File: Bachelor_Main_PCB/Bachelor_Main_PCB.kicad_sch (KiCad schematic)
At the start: 4 parts

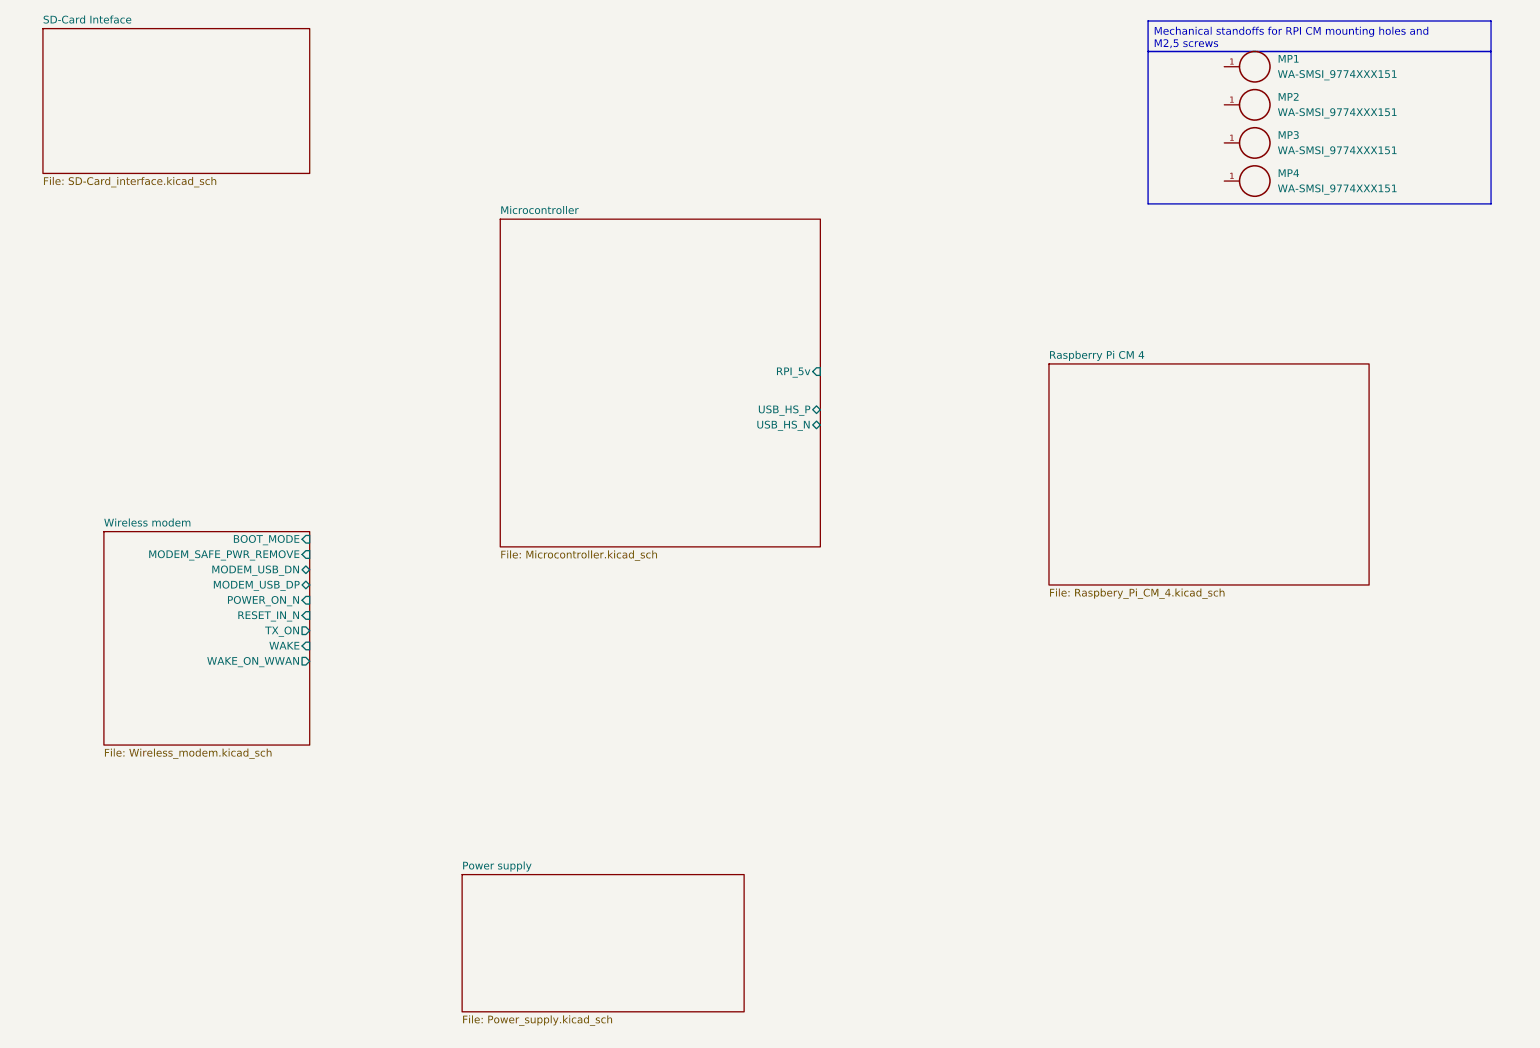
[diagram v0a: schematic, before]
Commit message: Add routing between hierarchal sheets modem and RPI
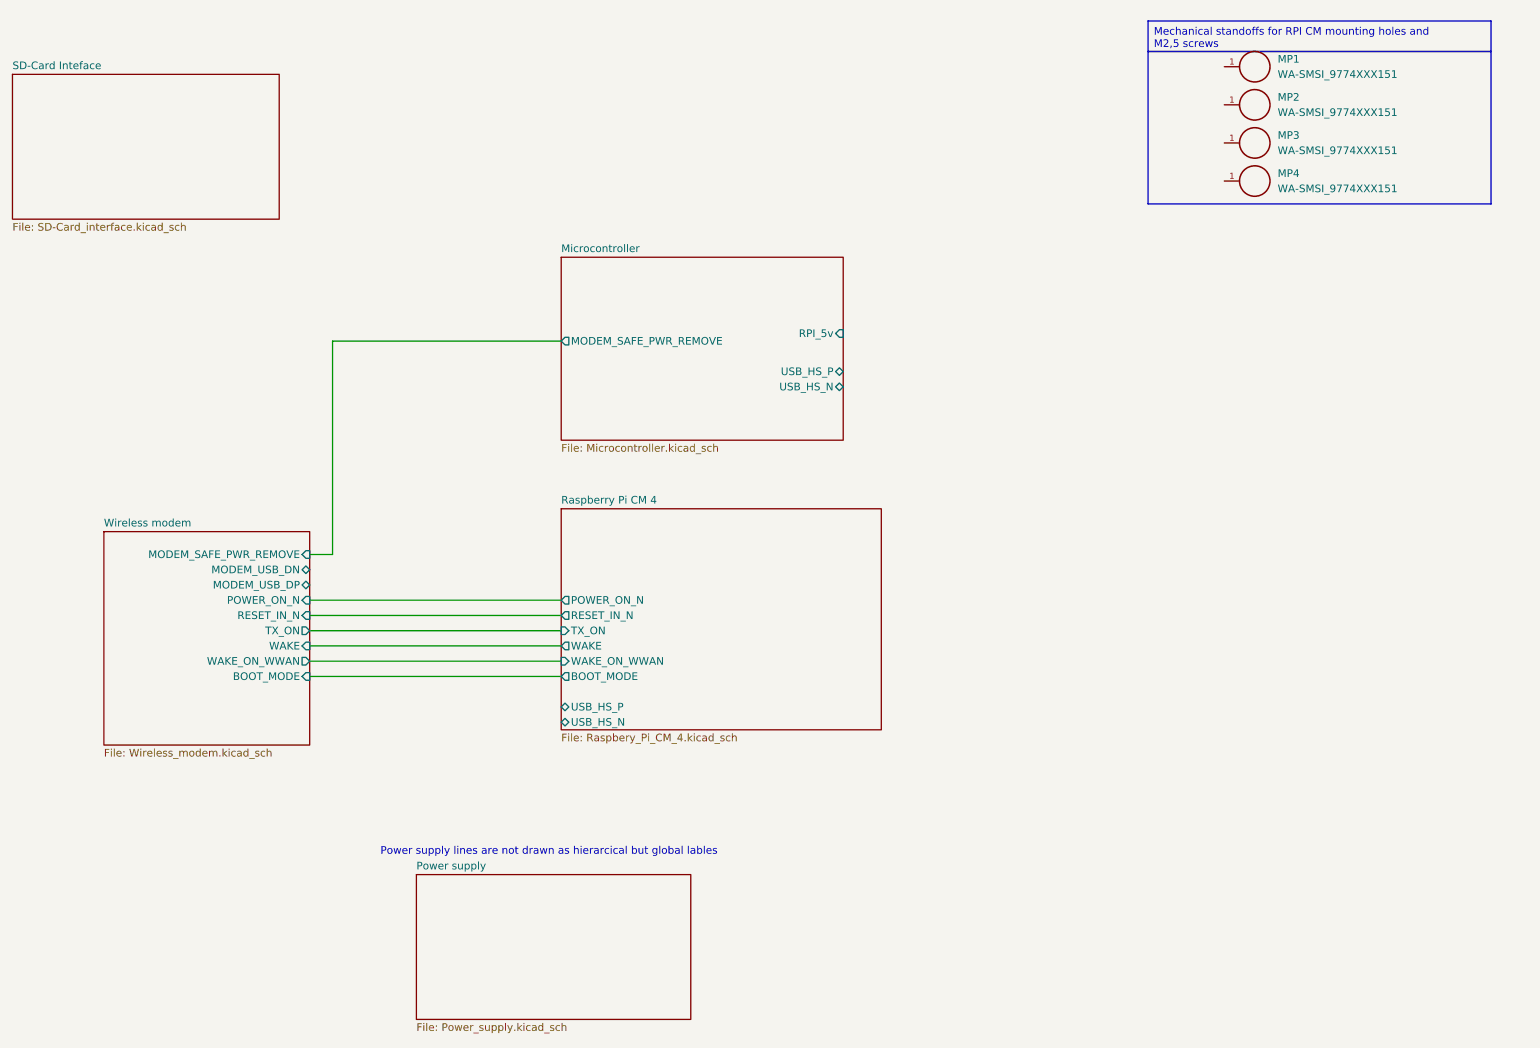
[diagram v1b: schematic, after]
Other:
- sheet Microcontroller ports: added MODEM_SAFE_PWR_REMOVE; removed none
- sheet Raspberry Pi CM 4 ports: added BOOT_MODE, POWER_ON_N, RESET_IN_N, TX_ON, USB_HS_N, USB_HS_P, WAKE, WAKE_ON_WWAN; removed none
- note added: "Power supply lines are not drawn as hierarcical but global lables"
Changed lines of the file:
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@@
 	(generator_version "9.0")
 	(paper "A4")
+	(text "Power supply lines are not drawn as hierarcical but global lables"
+		(exclude_from_sim no)
+		(at 119.888 156.21 0)
+		(effects
+			(font
+				(size 1.27 1.27)
+			)
+		)
+	)
 	(text_box " "
 		(exclude_from_sim no)
@@
 			)
 			(justify left top)
+		)
+	)
+	(wire
+		(pts
+			(xy 80.01 106.68) (xy 83.82 106.68)
+		)
+		(stroke
+			(width 0)
+			(type default)
+		)
+	)
+	(wire
+		(pts
+			(xy 83.82 71.12) (xy 121.92 71.12)
+		)
+		(stroke
+			(width 0)
+			(type default)
+		)
+	)
+	(wire
+		(pts
+			(xy 80.01 114.3) (xy 121.92 114.3)
+		)
+		(stroke
+			(width 0)
+			(type default)
+		)
+	)
+	(wire
+		(pts
+			(xy 80.01 127) (xy 121.92 127)
+		)
+		(stroke
+			(width 0)
+			(type default)
+		)
+	)
+	(wire
+		(pts
+			(xy 80.01 124.46) (xy 121.92 124.46)
+		)
+		(stroke
+			(width 0)
+			(type default)
+		)
+	)
+	(wire
+		(pts
+			(xy 83.82 106.68) (xy 83.82 71.12)
+		)
+		(stroke
+			(width 0)
+			(type default)
+		)
+	)
+	(wire
+		(pts
+			(xy 80.01 116.84) (xy 121.92 116.84)
+		)
+		(stroke
+			(width 0)
+			(type default)
+		)
+	)
+	(wire
+		(pts
+			(xy 80.01 121.92) (xy 121.92 121.92)
+		)
+		(stroke
+			(width 0)
+			(type default)
+		)
+	)
+	(wire
+		(pts
+			(xy 80.01 119.38) (xy 121.92 119.38)
+		)
+		(stroke
+			(width 0)
+			(type default)
 		)
 	)
@@
 		)
 		(pin "BOOT_MODE" input
-			(at 80.01 104.14 0)
+			(at 80.01 127 0)
 			(effects
 				(font
@@
 	)
 	(sheet
-		(at 203.2 74.93)
+		(at 121.92 99.06)
 		(size 53.34 36.83)
 		(exclude_from_sim no)
@@
 		)
 		(property "Sheetname" "Raspberry Pi CM 4"
-			(at 203.2 74.2184 0)
+			(at 121.92 98.3484 0)
 			(effects
 				(font
@@
 		)
 		(property "Sheetfile" "Raspbery_Pi_CM_4.kicad_sch"
-			(at 203.2 112.3446 0)
+			(at 121.92 136.4746 0)
 			(effects
 				(font
@@
 				)
 				(justify left top)
+			)
+		)
+		(pin "BOOT_MODE" output
+			(at 121.92 127 180)
+			(effects
+				(font
+					(size 1.27 1.27)
+				)
+				(justify left)
+			)
+		)
+		(pin "POWER_ON_N" output
+			(at 121.92 114.3 180)
+			(effects
+				(font
+					(size 1.27 1.27)
+				)
+				(justify left)
+			)
+		)
+		(pin "RESET_IN_N" output
+			(at 121.92 116.84 180)
+			(effects
+				(font
+					(size 1.27 1.27)
+				)
+				(justify left)
+			)
+		)
+		(pin "TX_ON" input
+			(at 121.92 119.38 180)
+			(effects
+				(font
+					(size 1.27 1.27)
+				)
+				(justify left)
+			)
+		)
+		(pin "USB_HS_N" bidirectional
+			(at 121.92 134.62 180)
+			(effects
+				(font
+					(size 1.27 1.27)
+				)
+				(justify left)
+			)
+		)
+		(pin "USB_HS_P" bidirectional
+			(at 121.92 132.08 180)
+			(effects
+				(font
+					(size 1.27 1.27)
+				)
+				(justify left)
+			)
+		)
+		(pin "WAKE" output
+			(at 121.92 121.92 180)
+			(effects
+				(font
+					(size 1.27 1.27)
+				)
+				(justify left)
+			)
+		)
+		(pin "WAKE_ON_WWAN" input
+			(at 121.92 124.46 180)
+			(effects
+				(font
+					(size 1.27 1.27)
+				)
+				(justify left)
 			)
 		)
@@
 	)
 	(sheet
-		(at 105.41 160.02)
-		(size 46.99 22.86)
+		(at 97.79 160.02)
+		(size 45.72 24.13)
 		(exclude_from_sim no)
 		(in_bom yes)
@@
 		)
 		(property "Sheetname" "Power supply"
-			(at 105.41 159.3084 0)
+			(at 97.79 159.3084 0)
 			(effects
 				(font
@@
 		)
 		(property "Sheetfile" "Power_supply.kicad_sch"
-			(at 105.41 183.4646 0)
+			(at 97.79 184.7346 0)
 			(effects
 				(font
@@
 	)
 	(sheet
-		(at 111.76 50.8)
-		(size 53.34 54.61)
+		(at 121.92 57.15)
+		(size 46.99 30.48)
 		(exclude_from_sim no)
 		(in_bom yes)
@@
 		)
 		(property "Sheetname" "Microcontroller"
-			(at 111.76 50.0884 0)
+			(at 121.92 56.4384 0)
 			(effects
 				(font
@@
 		)
 		(property "Sheetfile" "Microcontroller.kicad_sch"
-			(at 111.76 105.9946 0)
+			(at 121.92 88.2146 0)
 			(effects
 				(font
@@
 		)
 		(pin "RPI_5v" input
-			(at 165.1 76.2 0)
+			(at 168.91 69.85 0)
 			(effects
 				(font
@@
 		)
 		(pin "USB_HS_N" bidirectional
-			(at 165.1 85.09 0)
+			(at 168.91 78.74 0)
 			(effects
 				(font
@@
 		)
 		(pin "USB_HS_P" bidirectional
-			(at 165.1 82.55 0)
+			(at 168.91 76.2 0)
 			(effects
 				(font
@@
 				)
 				(justify right)
+			)
+		)
+		(pin "MODEM_SAFE_PWR_REMOVE" output
+			(at 121.92 71.12 180)
+			(effects
+				(font
+					(size 1.27 1.27)
+				)
+				(justify left)
 			)
 		)
@@
 	)
 	(sheet
-		(at 35.56 19.05)
+		(at 30.48 26.67)
 		(size 44.45 24.13)
 		(exclude_from_sim no)
@@
 		)
 		(property "Sheetname" "SD-Card Inteface"
-			(at 35.56 18.3384 0)
+			(at 30.48 25.9584 0)
 			(effects
 				(font
@@
 		)
 		(property "Sheetfile" "SD-Card_interface.kicad_sch"
-			(at 35.56 43.7646 0)
-			(effects
-				(font
+			(at 30.48 51.3846 0)
+			(effects
+				(font

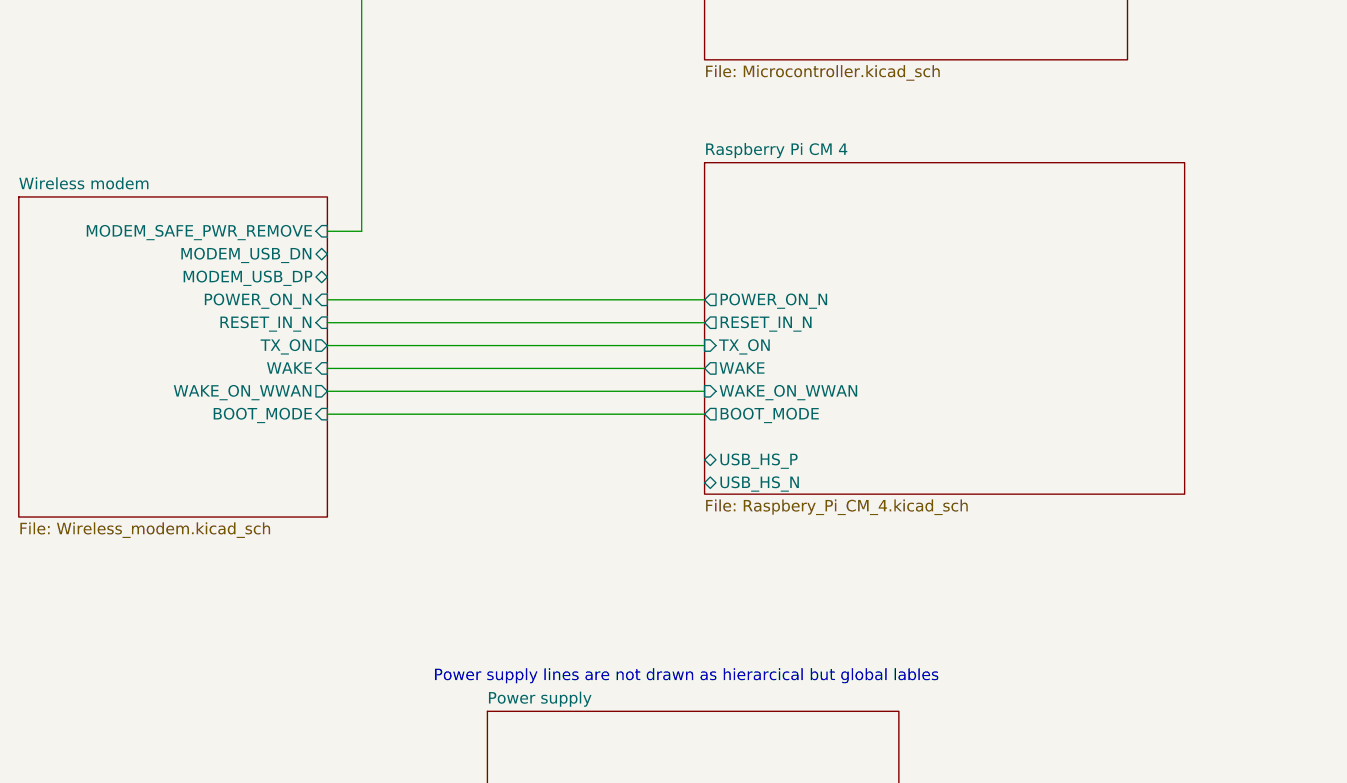
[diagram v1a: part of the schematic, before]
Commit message: Add MODEM_3V5_EN mosfet
Controlls the power supply to the modem from the RPI GPIO7
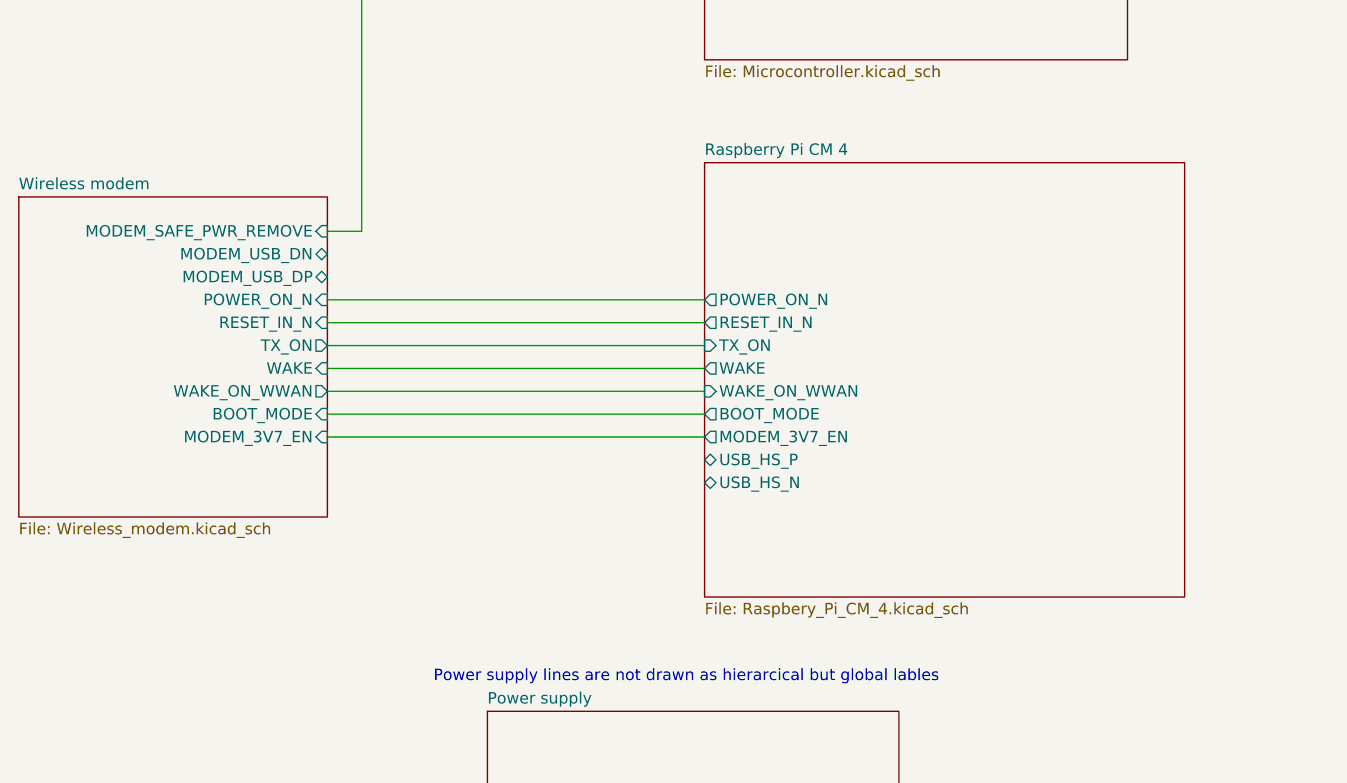
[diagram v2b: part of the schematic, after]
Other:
- sheet Raspberry Pi CM 4 ports: added MODEM_3V7_EN; removed none
- sheet Wireless modem ports: added MODEM_3V7_EN; removed none
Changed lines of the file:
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@@
+	(wire
+		(pts
+			(xy 80.01 129.54) (xy 121.92 129.54)
+		)
+		(stroke
+			(width 0)
+			(type default)
+		)
+	)
 	(wire
 		(pts
@@
 			)
 		)
+		(pin "MODEM_3V7_EN" input
+			(at 80.01 129.54 0)
+			(effects
+				(font
+					(size 1.27 1.27)
+				)
+				(justify right)
+			)
+		)
 		(instances
 			(project "Bachelor_Main_PCB"
@@
 	(sheet
 		(at 121.92 99.06)
-		(size 53.34 36.83)
+		(size 53.34 48.26)
 		(exclude_from_sim no)
 		(in_bom yes)
@@
 		)
 		(property "Sheetfile" "Raspbery_Pi_CM_4.kicad_sch"
-			(at 121.92 136.4746 0)
+			(at 121.92 147.9046 0)
 			(effects
 				(font
@@
 			(effects
 				(font
+					(size 1.27 1.27)
+				)
+				(justify left)
+			)
+		)
+		(pin "MODEM_3V7_EN" output
+			(at 121.92 129.54 180)
+			(effects
+				(font

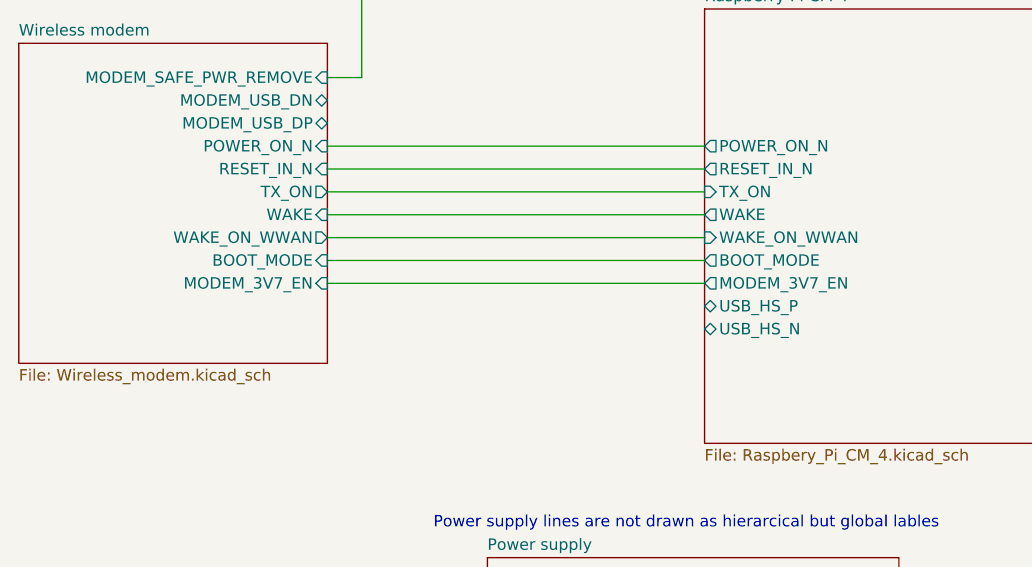
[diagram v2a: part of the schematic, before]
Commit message: Renamed wring MODEM_3V7_en to 3V5
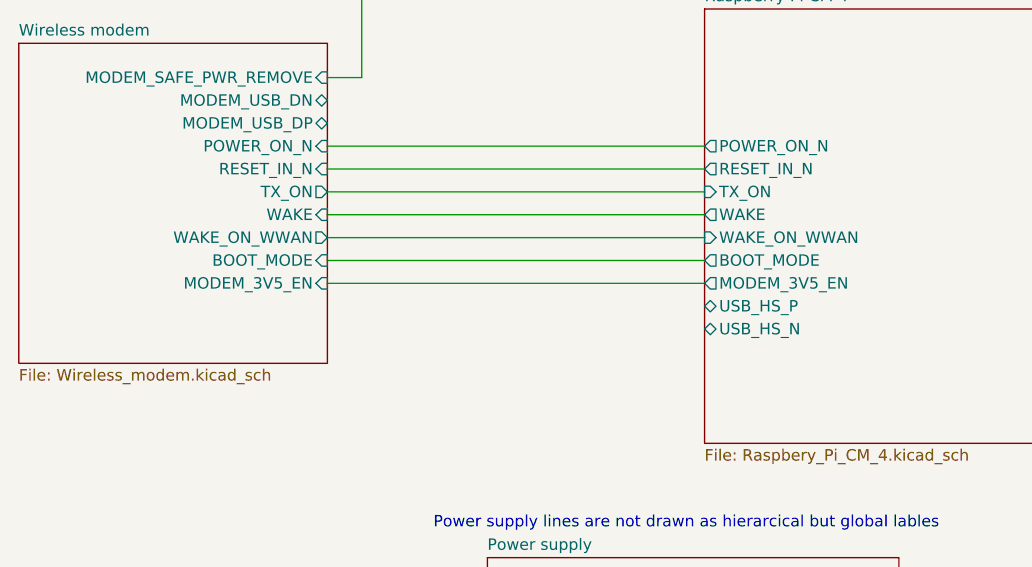
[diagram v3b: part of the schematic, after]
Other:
- sheet Raspberry Pi CM 4 ports: added MODEM_3V5_EN; removed MODEM_3V7_EN
- sheet Wireless modem ports: added MODEM_3V5_EN; removed MODEM_3V7_EN
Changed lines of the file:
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@@
 			)
 		)
-		(pin "MODEM_3V7_EN" input
+		(pin "MODEM_3V5_EN" input
 			(at 80.01 129.54 0)
 			(effects
@@
 			)
 		)
-		(pin "MODEM_3V7_EN" output
+		(pin "MODEM_3V5_EN" output
 			(at 121.92 129.54 180)
 			(effects

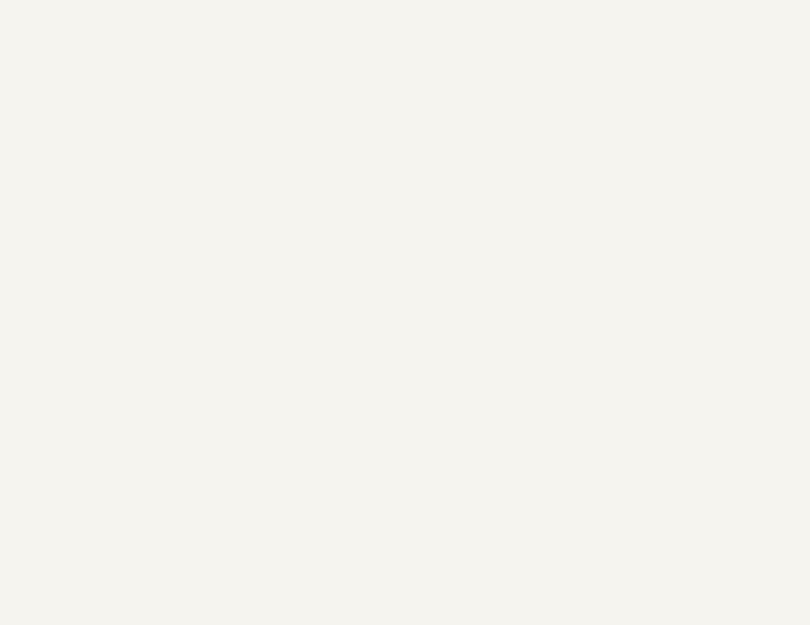
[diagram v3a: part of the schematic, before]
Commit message: Add USB HUB of type USB2514B-i/M2
Same as RPI CM 4 IO board
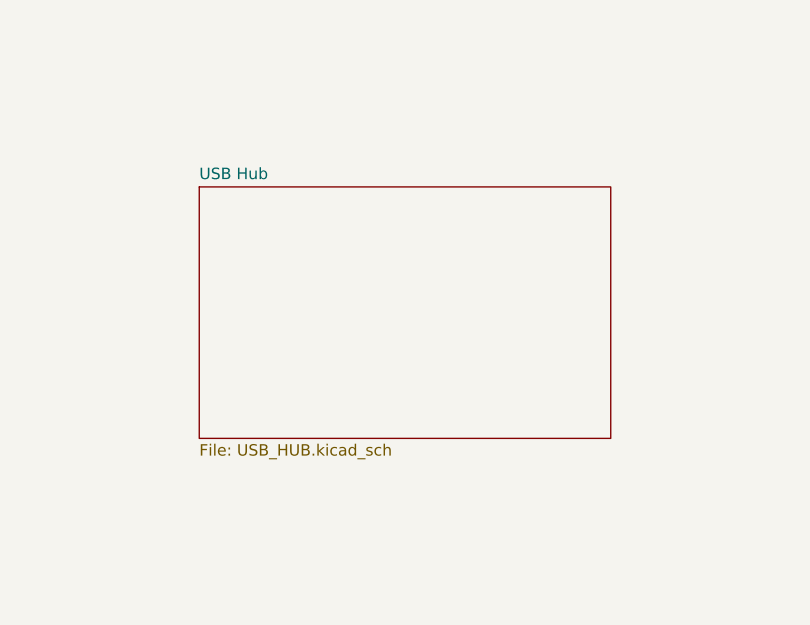
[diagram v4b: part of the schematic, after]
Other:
- added sheet USB Hub (USB_HUB.kicad_sch)
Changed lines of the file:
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@@
+	)
+	(sheet
+		(at 200.66 83.82)
+		(size 45.72 27.94)
+		(exclude_from_sim no)
+		(in_bom yes)
+		(on_board yes)
+		(dnp no)
+		(fields_autoplaced yes)
+		(stroke
+			(width 0.1524)
+			(type solid)
+		)
+		(fill
+			(color 0 0 0 0.0000)
+		)
+		(property "Sheetname" "USB Hub"
+			(at 200.66 83.1084 0)
+			(effects
+				(font
+					(size 1.27 1.27)
+				)
+				(justify left bottom)
+			)
+		)
+		(property "Sheetfile" "USB_HUB.kicad_sch"
+			(at 200.66 112.3446 0)
+			(effects
+				(font
+					(size 1.27 1.27)
+				)
+				(justify left top)
+			)
+		)
+		(instances
+			(project "Bachelor_Main_PCB"
+				(path "/3544d663-329e-4884-b753-28436ca187e8"
+					(page "7")
+				)
+			)
+		)
 	)
 	(sheet
